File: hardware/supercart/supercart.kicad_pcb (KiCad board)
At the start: 2 copper layers, 58 x 60 mm, 6 parts, among them J1 C64_EDGE_CONNECTOR_44, U1 ATF22V10C_SUPERCART, U2 AM29F080B_SO44

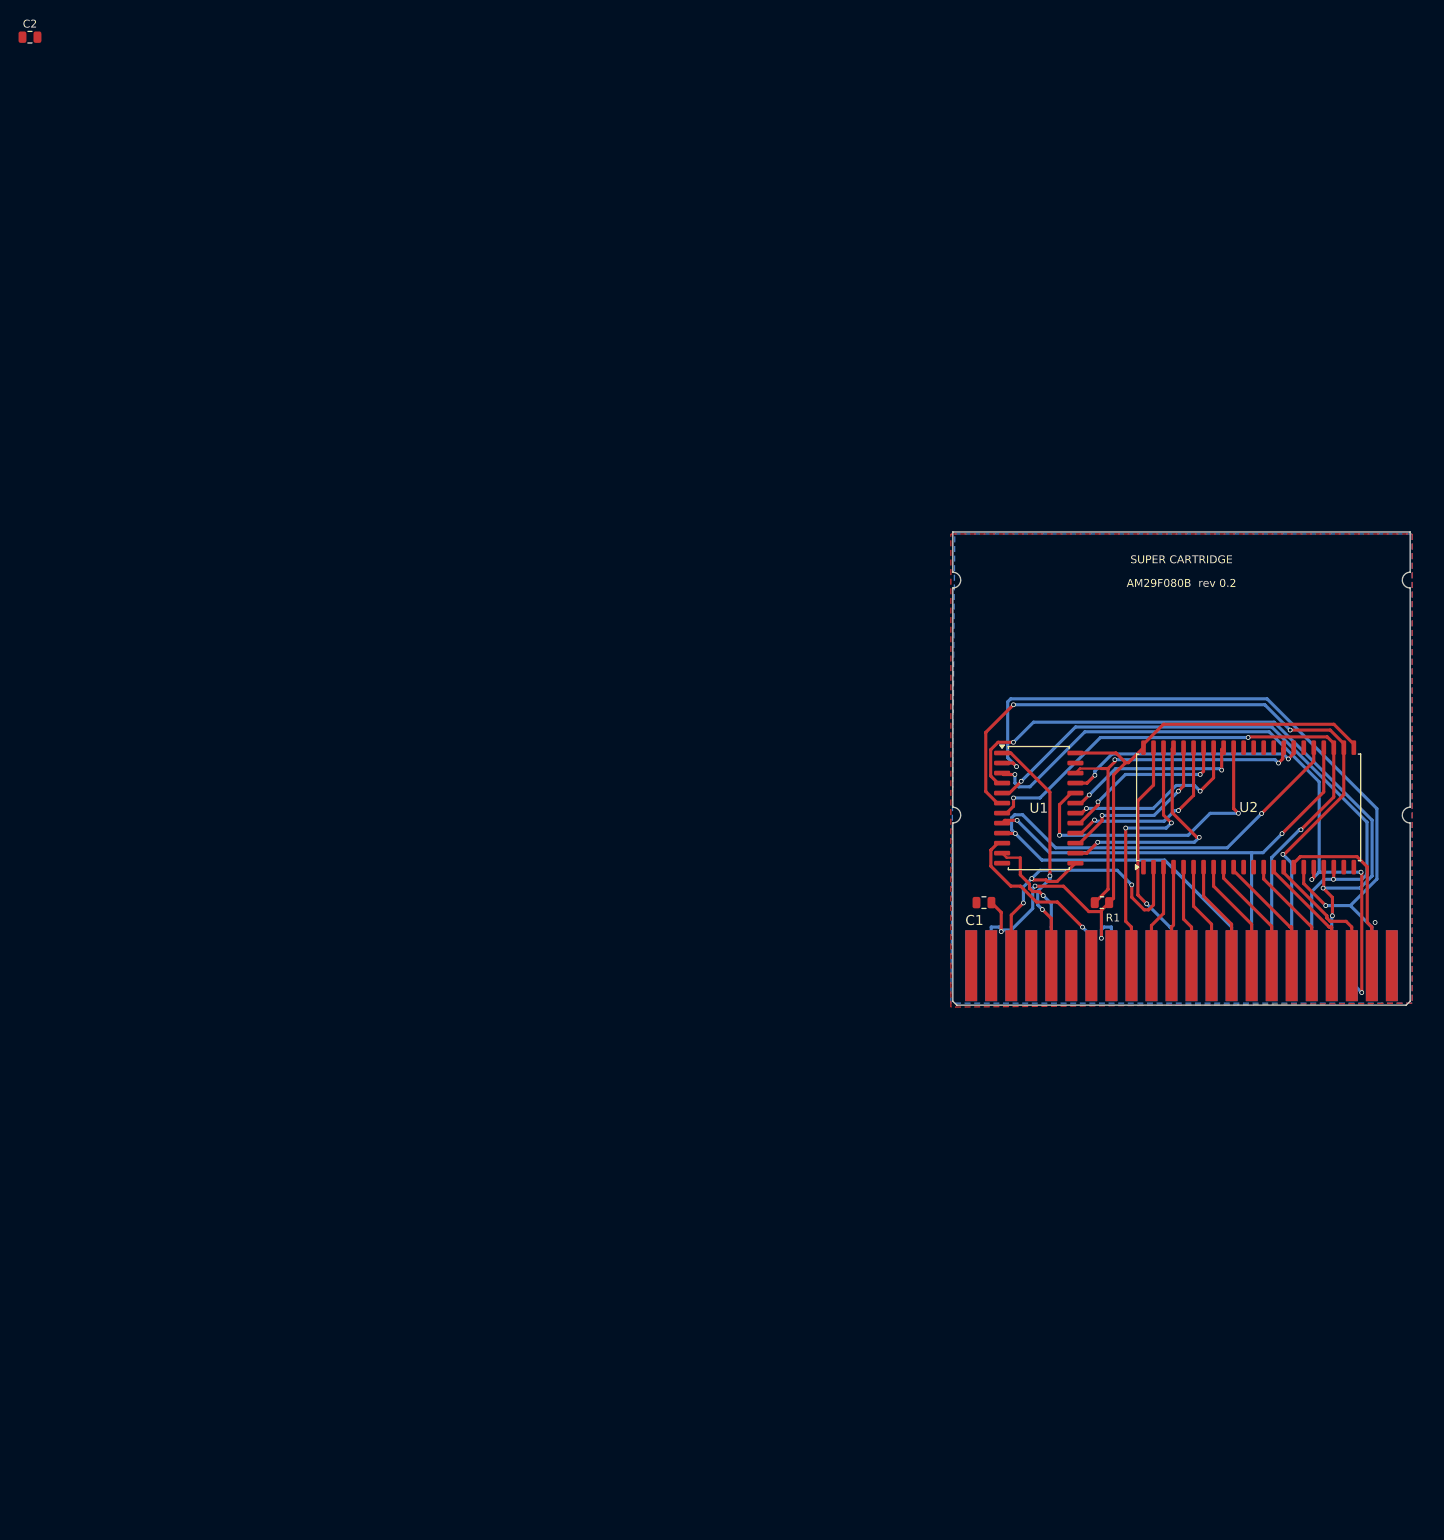
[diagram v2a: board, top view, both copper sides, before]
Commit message: Add ShackMate logo to SuperCart back silkscreen
Full logo (circuit-trace "SM" icon, "ShackMate" wordmark, and the
tagline) traced from branding/shackmate_logo_raw.png into a real
fabricatable footprint - nothing cropped or simplified.

Pipeline (scripts/make_shackmate_logo_footprint.py): ImageMagick
thresholds the source to pure black/white, potrace traces it to SVG,
then shapely+earcut correctly triangulate every hole (icon ring-dots,
both "a" counters, every "o"/"e" in the tagline) instead of naively
filling them solid. KiCad's own bitmap2component turned out to be
GUI-only in this KiCad 10 build (no headless batch mode found) and the
newer embedded-image footprint object doesn't actually export to
Gerbers (verified empirically - zero draw commands in the output) -
hence the custom pipeline.

Placed on B.SilkS (back silkscreen): the front is already full
(header text, both ICs, passives, connector) but the back was
completely empty, so the logo sits there at full size instead of
being squeezed to fit leftover front space. Coordinates are
pre-mirrored to KiCad's back-layer convention, confirmed correct by
rendering from both sides, not assumed.

Wired into gen_pcb.py so it survives future regenerations. This reset
supercart.kicad_pcb to placement-only (regeneration always rebuilds
from scratch) - the routing added since the last commit will need to
be redone; the pre-logo routed state is preserved in git history
(679c0c2) and backed up locally if needed.

Co-Authored-By: Claude Sonnet 5 <noreply@anthropic.com>
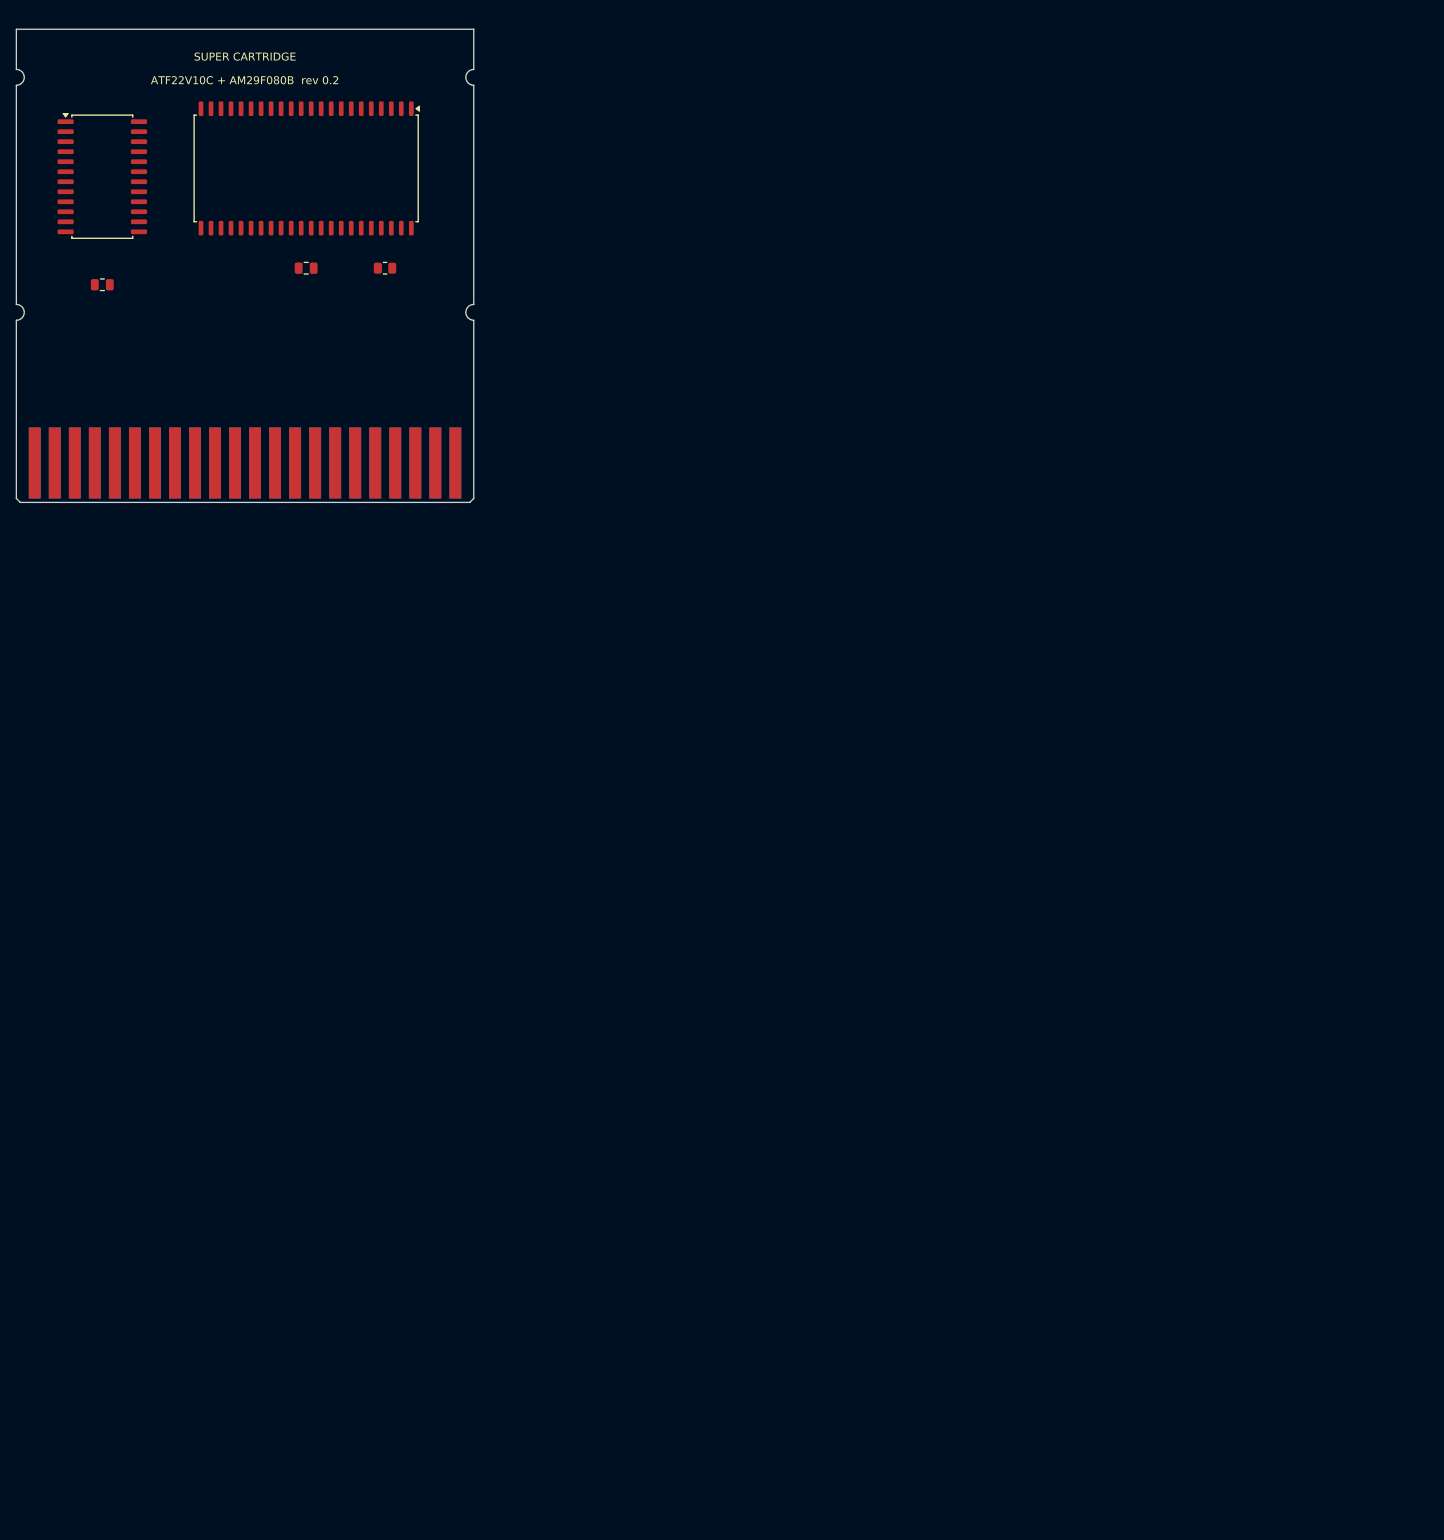
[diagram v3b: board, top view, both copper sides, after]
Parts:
- added ?: , supercart:SHACKMATE_LOGO, B.Cu at (29.0, 25.0)
- moved U2 144.4 mm to (36.8, 17.6), turned to 0 degrees
- moved U1 143.2 mm to (10.9, 18.7)
- moved C1 136.5 mm to (10.9, 32.4), turned to 0 degrees
- moved J1 134.8 mm to (29.0, 55.0)
- moved R1 121.4 mm to (46.8, 30.3), turned to 0 degrees
- moved C2 45.7 mm to (36.8, 30.3)
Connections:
- net /A0 renamed A0
- net /A1 renamed A1
- net /A10 renamed A10
- net /A11 renamed A11
- net /A12 renamed A12
- net /A2 renamed A2
- net /A3 renamed A3
- net /A4 renamed A4
- net /A5 renamed A5
- net /A6 renamed A6
- net /A7 renamed A7
- net /A8 renamed A8
- net /A9 renamed A9
- net /BANK0 renamed BANK0
- net /BANK1 renamed BANK1
- net /BANK2 renamed BANK2
- net /BANK3 renamed BANK3
- net /BANK4 renamed BANK4
- net /BANK5 renamed BANK5
- net /BANK6 renamed BANK6
- net /D0 renamed D0
- net /D1 renamed D1
- net /D2 renamed D2
- net /D3 renamed D3
- net /D4 renamed D4
- net /D5 renamed D5
- net /D6 renamed D6
- net /D7 renamed D7
- net /FLASH_OE_N renamed FLASH_OE_N
- net /FLASH_WE_N renamed FLASH_WE_N
- net /GND renamed GND
- net /IO1_N renamed IO1_N
- net /PHI2 renamed PHI2
- net /RESET_N renamed RESET_N
- net /ROML_N renamed ROML_N
- net /RW renamed RW
- net /TBD_FLASH_RYBY_N renamed TBD_FLASH_RYBY_N
- net /TBD_ROMH_N renamed TBD_ROMH_N
- net /VCC renamed VCC
- J1 pad 10: unconnected-(J1-IO2_N-Pad10) -> (no net)
- J1 pad 12: unconnected-(J1-BA-Pad12) -> (no net)
- J1 pad 13: unconnected-(J1-DMA_N-Pad13) -> (no net)
- J1 pad 4: unconnected-(J1-IRQ_N-Pad4) -> (no net)
- J1 pad 6: unconnected-(J1-DOTCLK-Pad6) -> (no net)
- J1 pad D: unconnected-(J1-NMI_N-PadD) -> (no net)
- J1 pad F: unconnected-(J1-A15-PadF) -> (no net)
- J1 pad H: unconnected-(J1-A14-PadH) -> (no net)
- J1 pad J: unconnected-(J1-A13-PadJ) -> (no net)
- U1 pad 23: unconnected-(U1-CTRL2-Pad23) -> (no net)
- U2 pad 1: unconnected-(U2-NC-Pad1) -> (no net)
- U2 pad 11: unconnected-(U2-NC-Pad11) -> (no net)
- U2 pad 12: unconnected-(U2-NC-Pad12) -> (no net)
- U2 pad 31: unconnected-(U2-NC-Pad31) -> (no net)
- U2 pad 32: unconnected-(U2-NC-Pad32) -> (no net)
- U2 pad 33: unconnected-(U2-NC-Pad33) -> (no net)
- U2 pad 34: unconnected-(U2-NC-Pad34) -> (no net)
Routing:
- net VCC: track 103.7 -> 0.00 mm, vias 3 -> 0
- net D0: track 95.0 -> 0.00 mm, vias 2 -> 0
- net D4: track 91.0 -> 0.00 mm, vias 3 -> 0
- net D7: track 87.6 -> 0.00 mm, vias 2 -> 0
- net D2: track 87.1 -> 0.00 mm, vias 3 -> 0
- net D1: track 86.1 -> 0.00 mm, vias 4 -> 0
- net D3: track 80.2 -> 0.00 mm, vias 2 -> 0
- net D5: track 78.6 -> 0.00 mm, vias 3 -> 0
- net D6: track 65.8 -> 0.00 mm, vias 2 -> 0
- net FLASH_WE_N: track 46.7 -> 0.00 mm, vias 2 -> 0
- net RESET_N: track 42.7 -> 0.00 mm, vias 3 -> 0
- net BANK6: track 38.9 -> 0.00 mm, vias 2 -> 0
- net A12: track 33.8 -> 0.00 mm, vias 2 -> 0
- net PHI2: track 31.5 -> 0.00 mm, vias 2 -> 0
- net FLASH_OE_N: track 30.8 -> 0.00 mm, vias 2 -> 0
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- removed copper zone on B.Cu, net GND
- removed copper zone on F.Cu, net GND
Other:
- board text added: "ATF22V10C + AM29F080B rev 0.2"
- board text added: "J1 F.Cu/B.Cu face assignment NOT"
- board text added: "TBD_* nets: Flash RY/BY# and J1 /ROMH"
- board text added: "not yet defined in PLD rev 0.2."
- board text added: "verified vs a real cartridge."
- board text removed: "AM29F080B rev 0.2"

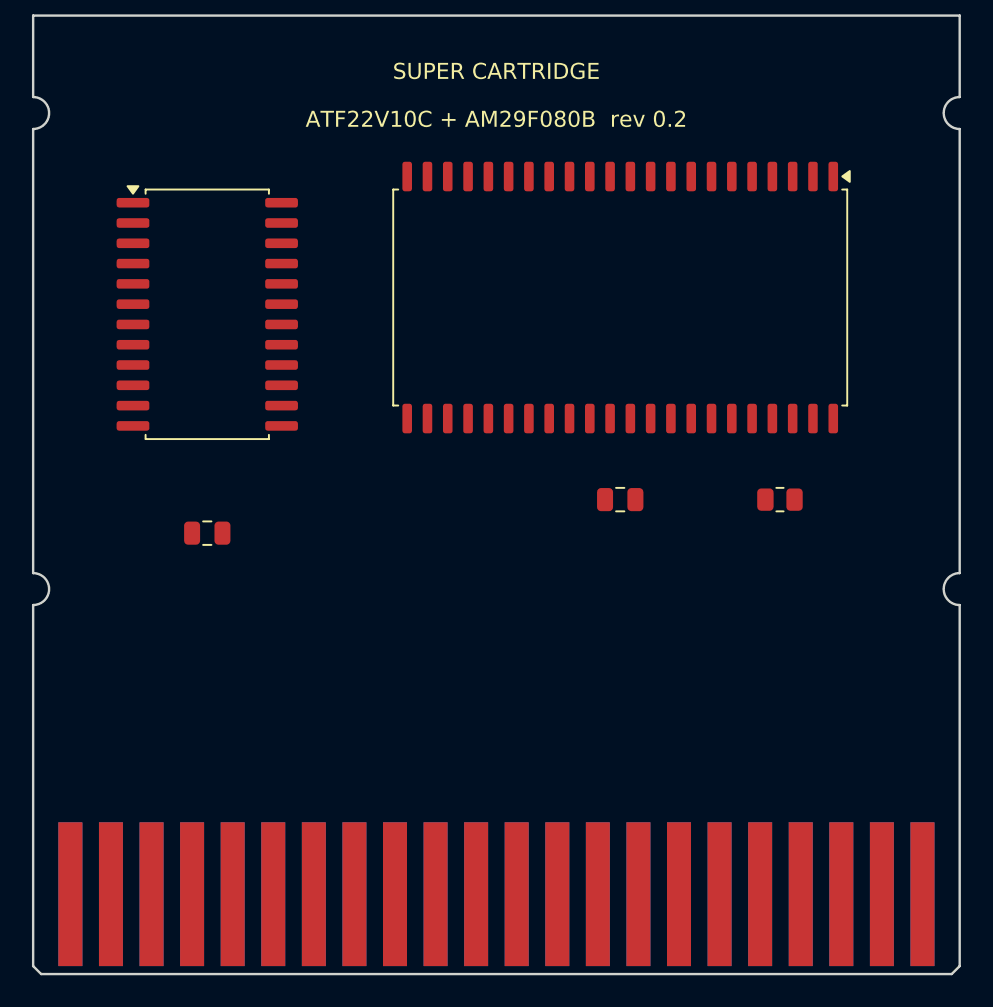
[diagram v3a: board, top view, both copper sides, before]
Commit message: Add PWR/WRITE/BUSY status LEDs and real 3D chip-marking text
Status LEDs (schematic + PCB): WRITE taps FLASH_WE_N, BUSY taps U2 pin 28
(RY/BY#) -- both real signals, both active-low, both buffered through
2N7002 MOSFETs wired as shunts across each LED (gate=0 lets a fixed
VCC->R->LED->GND path light it; gate=1 shorts it dark) rather than a
naive series switch, which would light the LED when idle instead of
when active -- verified against the truth table before wiring. RY/BY#
needed a new pull-up (R2): it's a real open-drain output per the
datasheet, previously unused and unpulled. PWR is a plain always-on
indicator. All current-limit resistors are 2.2k per spec; gate resistors
are 100R. Applied to the live schematic via load-and-append (preserves
GUI-edited state) rather than full regeneration.

3D IC body/marking (gen_pcb.py, scripts/make_ic_body_with_marking.py):
custom VRML bodies for U1/U2 with real laser-marking-style text raised
above the surface. Neither KiCad's 2D footprint text nor the VRML `Text`
node actually renders onto a 3D model's surface (both verified directly,
not assumed) -- real marking text requires actual mesh geometry, built
here by reusing the ShackMate logo's potrace/shapely/earcut pipeline in
3D instead of flat silkscreen. U2 also gets a real size fix: it was
previously a PSOP-44 substitute non-uniformly stretched to fit (no real
SO-44 3D model exists anywhere in KiCad's library), which visibly
distorted its corners/bevel; now an exact, undistorted 13.3x28.2mm body.
U1 trades its real, accurately-modeled stock SOIC body for a plainer
custom one to get the marking -- a real visual-fidelity tradeoff made
with explicit sign-off. Corrected "AM29F080B-90PD" (not a real ordering
code for this part -- only E=TSOP or S=SO exist) to the real "-90S".

Also: fix_reference_positions.py extended to hide reference-designator
silkscreen on the new small parts plus LOGO1 and J1 (packing 9 parts
into one 58x15mm strip made individual repositioning fragile; 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
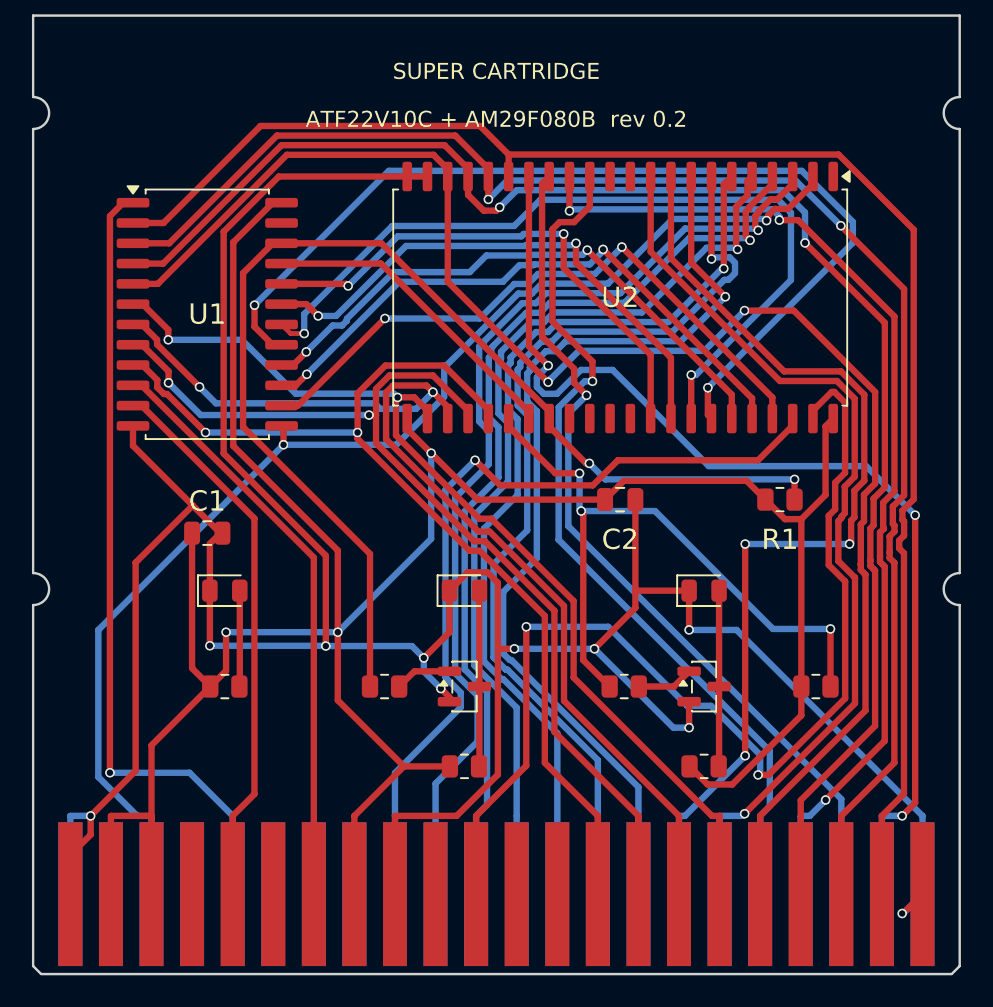
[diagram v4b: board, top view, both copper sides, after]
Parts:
- removed ?: , supercart:SHACKMATE_LOGO
- added LED1: LED_Green, LED_SMD:LED_0805_2012Metric, F.Cu at (12.0, 36.0)
- added LED2: LED_Red, LED_SMD:LED_0805_2012Metric, F.Cu at (27.0, 36.0)
- added LED3: LED_Amber, LED_SMD:LED_0805_2012Metric, F.Cu at (42.0, 36.0)
- added LOGO1: ShackMate, supercart:SHACKMATE_LOGO, B.Cu at (29.0, 25.0)
- added Q1: 2N7002, Package_TO_SOT_SMD:SOT-23, F.Cu at (27.0, 42.0)
- added Q2: 2N7002, Package_TO_SOT_SMD:SOT-23, F.Cu at (42.0, 42.0)
- added R2: 10k, Resistor_SMD:R_0805_2012Metric, F.Cu at (49.0, 42.0)
- added R3: 100, Resistor_SMD:R_0805_2012Metric, F.Cu at (22.0, 42.0)
- added R4: 100, Resistor_SMD:R_0805_2012Metric, F.Cu at (37.0, 42.0)
- added R5: 2.2k, Resistor_SMD:R_0805_2012Metric, F.Cu at (12.0, 42.0)
- added R6: 2.2k, Resistor_SMD:R_0805_2012Metric, F.Cu at (27.0, 47.0)
- added R7: 2.2k, Resistor_SMD:R_0805_2012Metric, F.Cu at (42.0, 47.0)
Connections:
- U2 pad 28: TBD_FLASH_RYBY_N -> FLASH_RYBY_N
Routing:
- net GND: track 0.00 -> 202.8 mm, vias 0 -> 10
- net VCC: track 0.00 -> 167.2 mm, vias 0 -> 3
- net D3: track 0.00 -> 98.5 mm, vias 0 -> 2
- net D0: track 0.00 -> 98.2 mm
- net D1: track 0.00 -> 97.0 mm, vias 0 -> 2
- net D2: track 0.00 -> 96.1 mm, vias 0 -> 2
- net RESET_N: track 0.00 -> 77.7 mm, vias 0 -> 2
- net FLASH_WE_N: track 0.00 -> 72.4 mm, vias 0 -> 2
- net A0: track 0.00 -> 67.5 mm, vias 0 -> 3
- net ROML_N: track 0.00 -> 67.4 mm, vias 0 -> 2
- net D5: track 0.00 -> 66.3 mm, vias 0 -> 2
- net A2: track 0.00 -> 64.7 mm, vias 0 -> 3
- net D7: track 0.00 -> 64.6 mm, vias 0 -> 2
- net D6: track 0.00 -> 63.8 mm, vias 0 -> 2
- net D4: track 0.00 -> 62.3 mm, vias 0 -> 2
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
